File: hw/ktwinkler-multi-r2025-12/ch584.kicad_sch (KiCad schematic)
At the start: 10 parts, among them J10 Conn_01x06, SW4 BOOT, SW6 RESET_CH, U8 CH584F, Y1 Q13FC13500004, Y4 Crystal_32M_2016_XTM20032000D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

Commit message: ready for scope creep
I think the schematic is ... mostly ok?  I need to decide how much of
the han p1 port scope creep to bother doing, or not...

I've roughyl blocked out the board, seems as good as any?
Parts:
- removed R17, R18: 0R, Resistor_SMD:R_0402_1005Metric, symbol karl-atomic-basic:KR0402_22R
- removed SW4: BOOT, Button_Switch_SMD:SW_SPST_TL3342, symbol Switch:SW_Push
- removed SW6: RESET_CH, Button_Switch_SMD:SW_SPST_TL3342, symbol Switch:SW_Push
- removed Y1: Q13FC13500004, Crystal:Crystal_SMD_3215-2Pin_3.2x1.5mm, symbol karl-atomic-basic:Q13FC13500004
- removed Y4: Crystal_32M_2016_XTM20032000DT00351005, Crystal:Crystal_SMD_2016-4Pin_2.0x1.6mm, symbol karl-parts:Crystal_32M_2016_XTM20032000DT00351005
- added C19, C22: 1uF, Capacitor_SMD:C_0603_1608Metric, symbol karl-atomic-basic:KC0603_1uF
- added C20: 100nF, Capacitor_SMD:C_0402_1005Metric, symbol karl-atomic-basic:KC0402_100nF_16V
- added J3: Conn_01x04, Connector_PinHeader_2.54mm:PinHeader_1x04_P2.54mm_Vertical, symbol Connector_Generic:Conn_01x04
- added Y4: 32k, Crystal:Crystal_SMD_3215-2Pin_3.2x1.5mm, symbol karl-atomic-basic:Crystal_32k_3215_Q13FC13500004
- added Y5: 32M, Crystal:Crystal_SMD_2016-4Pin_2.0x1.6mm, symbol karl-parts:Crystal_32M_2016_XTM20032000DT00351005
- U8: footprint (none) -> Package_DFN_QFN:QFN-32-1EP_4x4mm_P0.4mm_EP2.65x2.65mm; LCSC Part # (none) -> C42381468; MPN (none) -> CH584F
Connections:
- net GND: now also C19.2, C20.2, C22.2, Y5.1, Y5.3
- net USBDM: now also U8.14 (PB10_U1DN_TMR1)
- net USBDP: now also U8.13 (PB11_U1DP_TMR2)
- net clki: now also Y5.4
- net clko: now also Y5.2
- net at U8.1 (PA10_X32KI_TMR1): now also Y4.2
- net at U8.2 (VDCID): now also U8.25 (VDCIA), U8.3 (VSW), C19.1
- net at U8.23 (VINTA): now also C22.1
- net at U8.32 (PA11_X32KO_TMR2): now also Y4.1
- net at U8.4 (VIO33_VDD33): now also C20.1
- net TWI_SCL: now reaches U8.11 (PB13_U2DP_SCK0_SCL_TXD1)
- net TWI_SCL: now also J3.1 (Pin_1)
- net TWI_SDA: now reaches U8.12 (PB12_U2DM_SCS_SDA_RXD1)
- net TWI_SDA: now also J3.2 (Pin_2)
- net BOOT: now reaches U8.20 (PB22_TMR3_RXD2)
- net at U8.26 (PA4_RXD3_AIN0): now also J3.3 (Pin_3)
- net at U8.27 (PA5_TXD3_AIN1): now also J3.4 (Pin_4)
- net PWM6 renamed RESET_CH5x
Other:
- note added: "Make this a stemma/qwiic/compat? this is for "reuse this board""
- note added: "meh, do I want to do the DCDC support? You know what, no. I'm not wiring up all the faff for measuring current on both parts, forget it."

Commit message: this is just getting silly
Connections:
- net PWM3 renamed P1IN
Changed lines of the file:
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@@
+	(wire
+		(pts
+			(xy 106.68 116.84) (xy 106.68 121.92)
+		)
+		(stroke
+			(width 0)
+			(type default)
+		)
+	)
 	(wire
 		(pts
@@
 	(wire
 		(pts
+			(xy 106.68 121.92) (xy 119.38 121.92)
+		)
+		(stroke
+			(width 0)
+			(type default)
+		)
+	)
+	(wire
+		(pts
 			(xy 124.46 45.72) (xy 119.38 45.72)
 		)
@@
 	(wire
 		(pts
+			(xy 43.18 116.84) (xy 106.68 116.84)
+		)
+		(stroke
+			(width 0)
+			(type default)
+		)
+	)
+	(wire
+		(pts
 			(xy 185.42 106.68) (xy 193.04 106.68)
 		)
@@
 		(pts
 			(xy 170.18 111.76) (xy 185.42 111.76)
+		)
+		(stroke
+			(width 0)
+			(type default)
+		)
+	)
+	(wire
+		(pts
+			(xy 119.38 121.92) (xy 119.38 124.46)
 		)
 		(stroke
@@
 		(effects
 			(font
+				(size 1.27 1.27)
+			)
+			(justify right)
+		)
+	)
+	(hierarchical_label "P1IN"
+		(shape input)
+		(at 43.18 116.84 180)
+		(effects
+			(font

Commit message: "schematic complete" (lol)
but yeah, i think this is most of it?  time to maybe route shit?
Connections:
- net PWM5 renamed P1_Req_Out
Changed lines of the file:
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@@
+	(wire
+		(pts
+			(xy 50.8 119.38) (xy 43.18 119.38)
+		)
+		(stroke
+			(width 0)
+			(type default)
+		)
+	)
 	(wire
 		(pts
@@
 	(label "TIO"
 		(at 138.43 182.88 0)
+		(effects
+			(font
+				(size 1.27 1.27)
+			)
+			(justify left bottom)
+		)
+	)
+	(label "PWM5"
+		(at 50.8 119.38 0)
 		(effects
 			(font
@@
 		(shape output)
 		(at 33.02 101.6 180)
+		(effects
+			(font
+				(size 1.27 1.27)
+			)
+			(justify right)
+		)
+	)
+	(hierarchical_label "P1_Req_Out"
+		(shape output)
+		(at 43.18 119.38 180)
 		(effects
 			(font
@@
 	)
 	(symbol
-		(lib_name "CH584F_1")
+		(lib_name "CH584F_2")
 		(lib_id "wch-bluetooth:CH584F")
 		(at 142.24 45.72 0)
@@
 	)
 	(symbol
+		(lib_name "CH584F_1")
 		(lib_id "wch-bluetooth:CH584F")
 		(at 147.32 119.38 0)

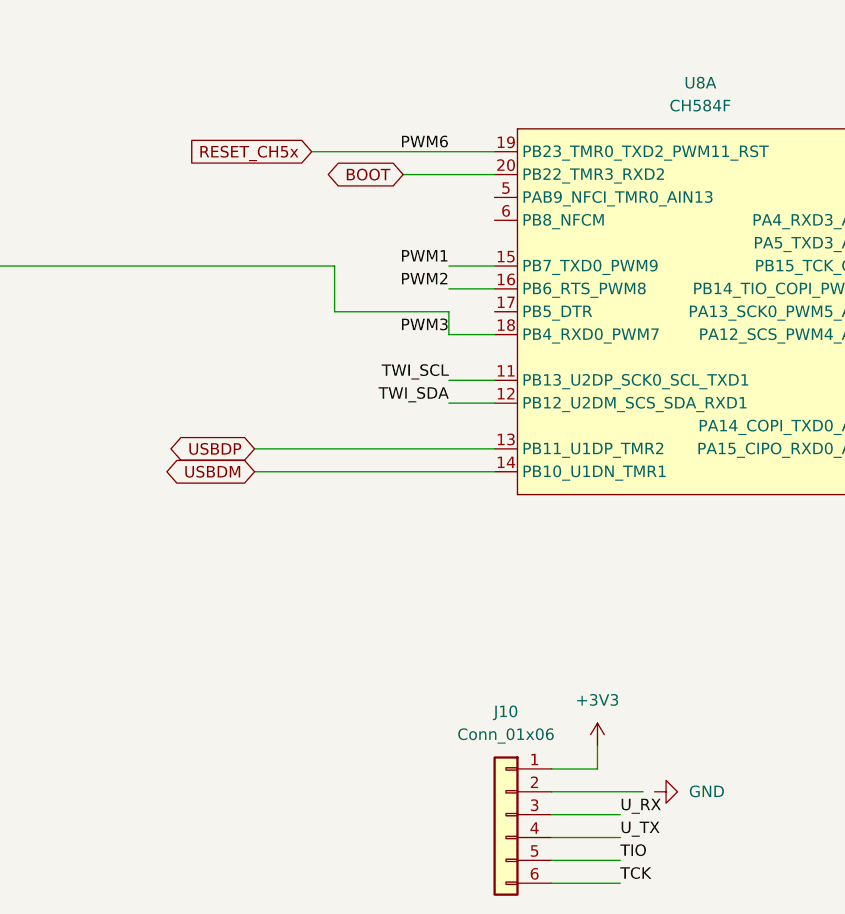
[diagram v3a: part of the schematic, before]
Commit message: update following ERC and symbol fixes
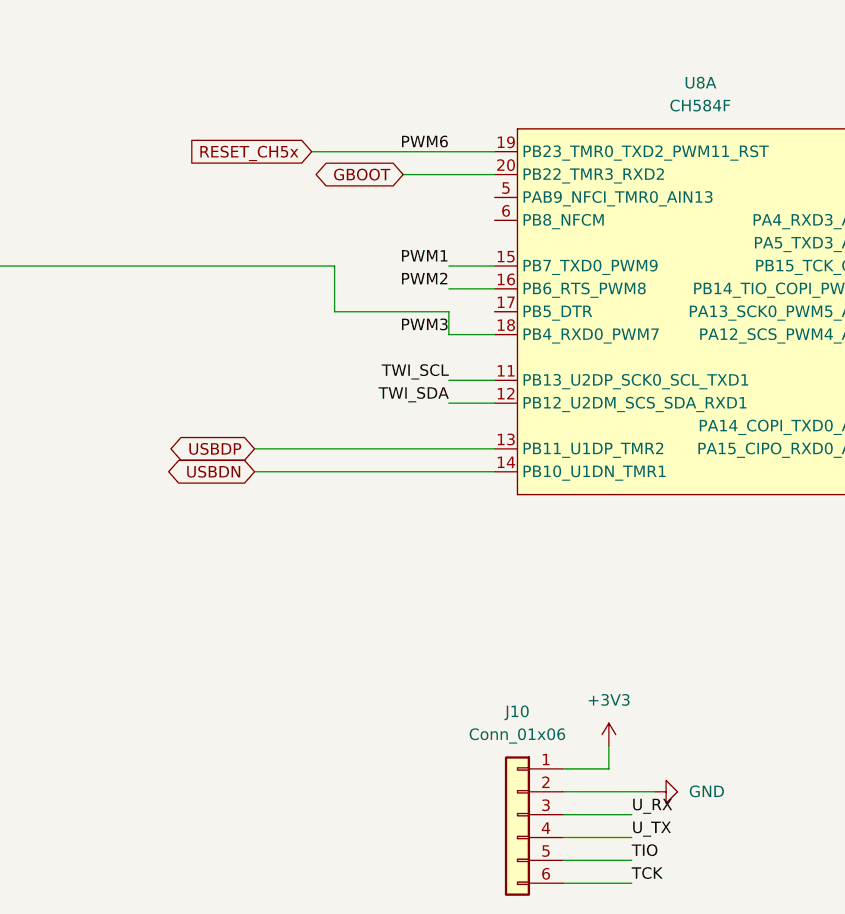
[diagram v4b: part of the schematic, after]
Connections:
- net GND: now also J10.2 (Pin_2)
- net BOOT renamed GBOOT
- net USBDM renamed USBDN
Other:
- moved on the sheet: J10
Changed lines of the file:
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@@
 	(wire
 		(pts
-			(xy 130.81 180.34) (xy 138.43 180.34)
+			(xy 132.08 180.34) (xy 139.7 180.34)
 		)
 		(stroke
@@
 	(wire
 		(pts
-			(xy 130.81 172.72) (xy 135.89 172.72)
-		)
-		(stroke
-			(width 0)
-			(type default)
-		)
-	)
-	(wire
-		(pts
-			(xy 130.81 175.26) (xy 140.97 175.26)
+			(xy 132.08 172.72) (xy 137.16 172.72)
+		)
+		(stroke
+			(width 0)
+			(type default)
+		)
+	)
+	(wire
+		(pts
+			(xy 132.08 175.26) (xy 142.24 175.26)
 		)
 		(stroke
@@
 	(wire
 		(pts
-			(xy 130.81 185.42) (xy 138.43 185.42)
+			(xy 132.08 185.42) (xy 139.7 185.42)
 		)
 		(stroke
@@
 	(wire
 		(pts
-			(xy 130.81 182.88) (xy 138.43 182.88)
+			(xy 132.08 182.88) (xy 139.7 182.88)
 		)
 		(stroke
@@
 	(wire
 		(pts
-			(xy 130.81 177.8) (xy 138.43 177.8)
-		)
-		(stroke
-			(width 0)
-			(type default)
-		)
-	)
-	(wire
-		(pts
-			(xy 135.89 172.72) (xy 135.89 170.18)
+			(xy 132.08 177.8) (xy 139.7 177.8)
+		)
+		(stroke
+			(width 0)
+			(type default)
+		)
+	)
+	(wire
+		(pts
+			(xy 137.16 172.72) (xy 137.16 170.18)
 		)
 		(stroke
@@
 	)
 	(label "U_TX"
-		(at 138.43 180.34 0)
+		(at 139.7 180.34 0)
 		(effects
 			(font
@@
 	)
 	(label "U_RX"
-		(at 138.43 177.8 0)
+		(at 139.7 177.8 0)
 		(effects
 			(font
@@
 	)
 	(label "TIO"
-		(at 138.43 182.88 0)
+		(at 139.7 182.88 0)
 		(effects
 			(font
@@
 	)
 	(label "TCK"
-		(at 138.43 185.42 0)
+		(at 139.7 185.42 0)
 		(effects
 			(font
@@
 		)
 	)
-	(global_label "USBDM"
+	(global_label "USBDN"
 		(shape bidirectional)
 		(at 97.79 139.7 180)
@@
 		)
 		(property "Intersheetrefs" "${INTERSHEET_REFS}"
-			(at 87.1621 139.7 0)
+			(at 87.283 139.7 0)
 			(effects
 				(font
@@
 		)
 	)
-	(global_label "BOOT"
+	(global_label "GBOOT"
 		(shape bidirectional)
 		(at 114.3 106.68 180)
@@
 		)
 		(property "Intersheetrefs" "${INTERSHEET_REFS}"
-			(at 105.3049 106.68 0)
+			(at 104.0349 106.68 0)
 			(effects
 				(font
@@
 	(symbol
 		(lib_id "Connector_Generic:Conn_01x06")
-		(at 125.73 177.8 0)
+		(at 127 177.8 0)
 		(mirror y)
 		(unit 1)
@@
 		(fields_autoplaced yes)
 		(property "Reference" "J10"
-			(at 125.73 166.37 0)
+			(at 127 166.37 0)
 			(effects
 				(font
@@
 		)
 		(property "Value" "Conn_01x06"
-			(at 125.73 168.91 0)
+			(at 127 168.91 0)
 			(effects
 				(font
@@
 		)
 		(property "Footprint" "Connector_PinHeader_2.54mm:PinHeader_1x06_P2.54mm_Vertical"
-			(at 125.73 177.8 0)
+			(at 127 177.8 0)
 			(effects
 				(font
@@
 		)
 		(property "Datasheet" "~"
-			(at 125.73 177.8 0)
+			(at 127 177.8 0)
 			(effects
 				(font
@@
 		)
 		(property "Description" "Generic connector, single row, 01x06, script generated (kicad-library-utils/schlib/autogen/connector/)"
-			(at 125.73 177.8 0)
+			(at 127 177.8 0)
 			(effects
 				(font
@@
 	(symbol
 		(lib_id "power:+3V3")
-		(at 135.89 170.18 0)
+		(at 137.16 170.18 0)
 		(unit 1)
 		(exclude_from_sim no)
@@
 		(fields_autoplaced yes)
 		(property "Reference" "#PWR042"
-			(at 135.89 173.99 0)
+			(at 137.16 173.99 0)
 			(effects
 				(font
@@
 		)
 		(property "Value" "+3V3"
-			(at 135.89 165.1 0)
+			(at 137.16 165.1 0)
 			(effects
 				(font
@@
 		)
 		(property "Footprint" ""
-			(at 135.89 170.18 0)
+			(at 137.16 170.18 0)
 			(effects
 				(font
@@
 		)
 		(property "Datasheet" ""
-			(at 135.89 170.18 0)
+			(at 137.16 170.18 0)
 			(effects
 				(font
@@
 		)
 		(property "Description" "Power symbol creates a global label with name \"+3V3\""
-			(at 135.89 170.18 0)
+			(at 137.16 170.18 0)
 			(effects
 				(font
@@
 	)
 	(symbol
-		(lib_name "CH584F_1")
 		(lib_id "wch-bluetooth:CH584F")
 		(at 147.32 119.38 0)

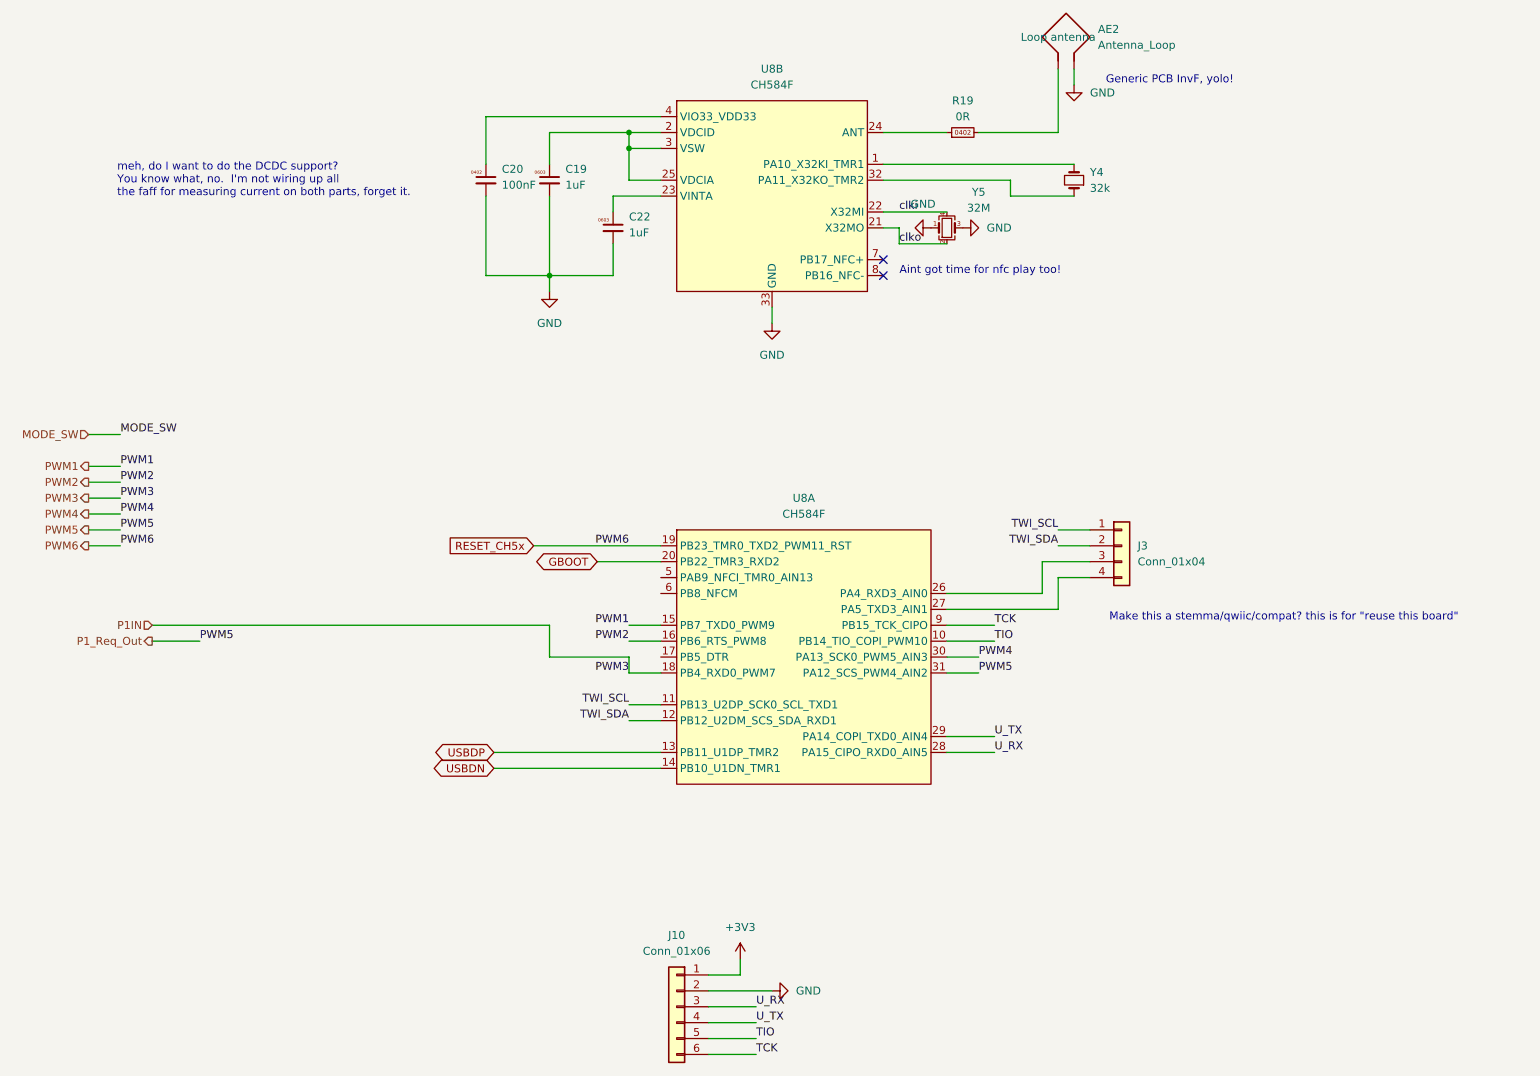
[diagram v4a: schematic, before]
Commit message: streammmm updates
"complete" apart from finishing those antennas.
needs DRC cleanups on both the wch inv-f and also the yolo-pole.
need to at least _basically_ get the antenna trace basic wdith correct
as well.  yolo is fine, when it's guided yolo, not "lol"
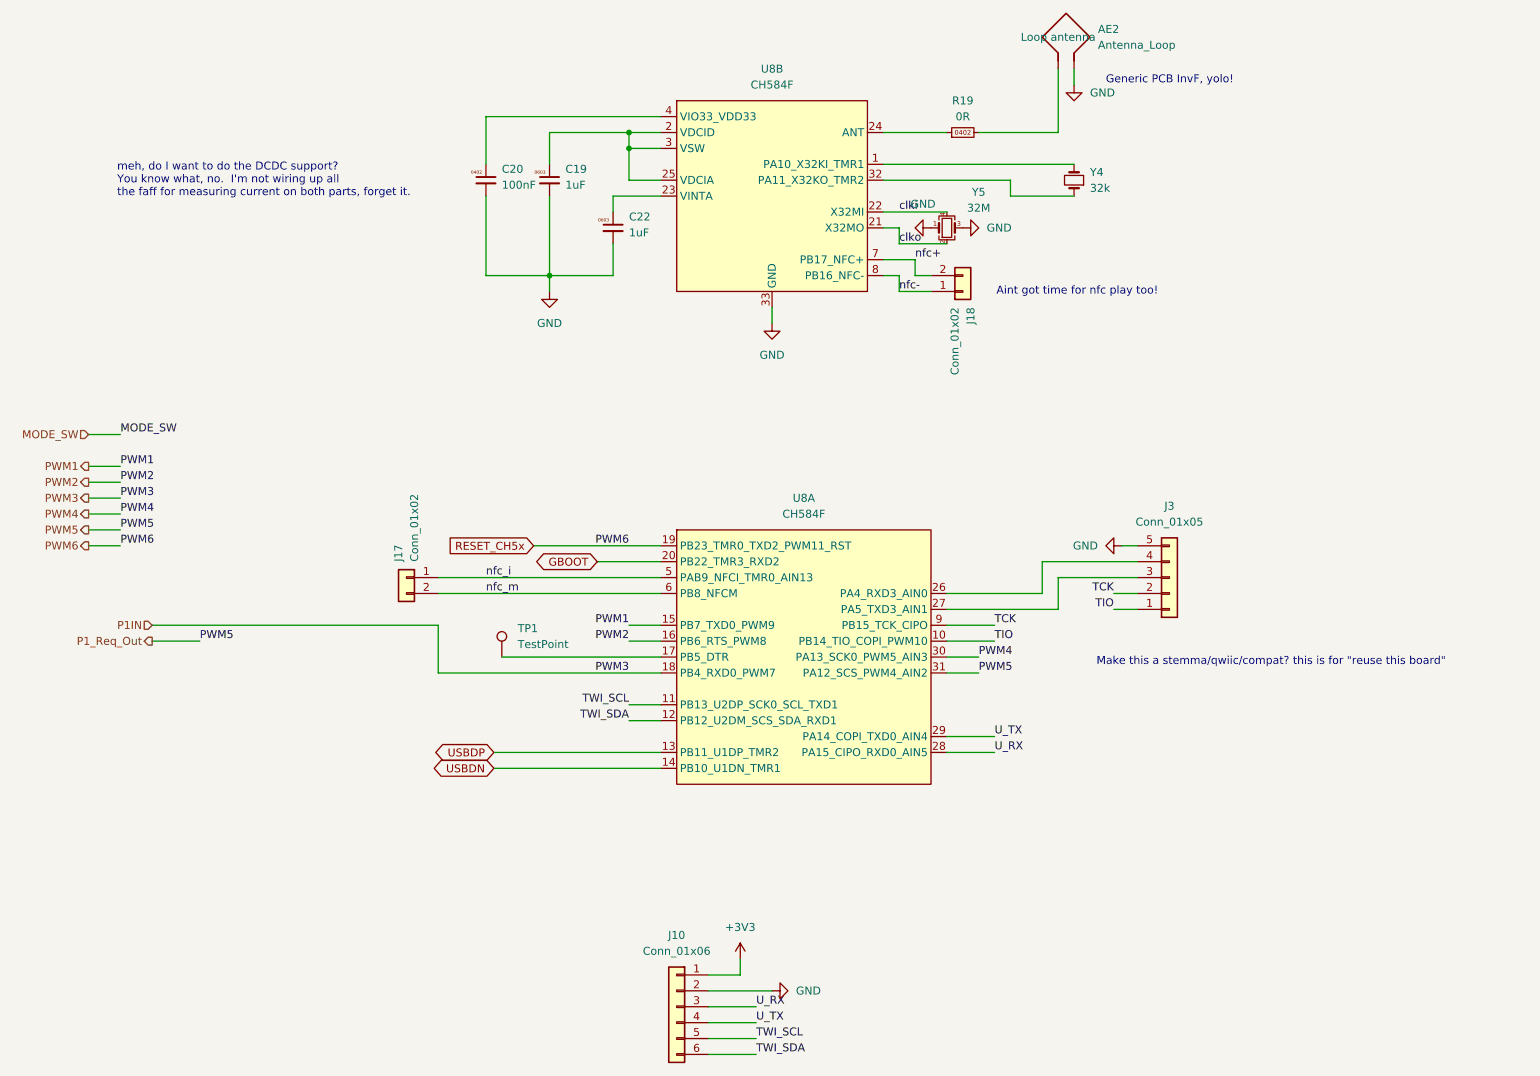
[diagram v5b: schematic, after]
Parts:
- removed J3: Conn_01x04, Connector_PinHeader_2.54mm:PinHeader_1x04_P2.54mm_Vertical, symbol Connector_Generic:Conn_01x04
- added J17, J18: Conn_01x02, TestPoint:TestPoint_2Pads_Pitch2.54mm_Drill0.8mm, symbol Connector_Generic:Conn_01x02
- added J3: Conn_01x05, Connector_PinHeader_2.54mm:PinHeader_1x05_P2.54mm_Vertical, symbol Connector_Generic:Conn_01x05
- added TP1: TestPoint, TestPoint:TestPoint_THTPad_D1.0mm_Drill0.5mm, symbol Connector:TestPoint
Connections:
- net GND: now also J3.5 (Pin_5)
- net TCK: now also J3.2 (Pin_2); no longer J10.6 (Pin_6)
- net TIO: now also J3.1 (Pin_1); no longer J10.5 (Pin_5)
- net TWI_SCL: now also J10.5 (Pin_5)
- net TWI_SDA: now also J10.6 (Pin_6)
- net at U8.26 (PA4_RXD3_AIN0): now also J3.4 (Pin_4)
- net at U8.27 (PA5_TXD3_AIN1): now also J3.3 (Pin_3)
- net nfc+: now reaches U8.7 (PB17_NFC+)
- net nfc+: now also J18.2 (Pin_2)
- net nfc-: now reaches U8.8 (PB16_NFC-)
- net nfc-: now also J18.1 (Pin_1)
- net at U8.17 (PB5_DTR): now also TP1.1
- net nfc_i: now reaches U8.5 (PAB9_NFCI_TMR0_AIN13)
- net nfc_i: now also J17.1 (Pin_1)
- net nfc_m: now reaches U8.6 (PB8_NFCM)
- net nfc_m: now also J17.2 (Pin_2)
- no-connect marks 2 -> 0
